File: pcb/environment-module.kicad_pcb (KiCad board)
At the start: 4 copper layers, 50 x 25 mm, 100 parts, among them J1 AVR-UPDI-6, U1 ATtiny1616-MNR, U2 PCA9545APW, U3 AHT20-F, U4 LTR-303ALS-01, U5 SGP40-D-R4

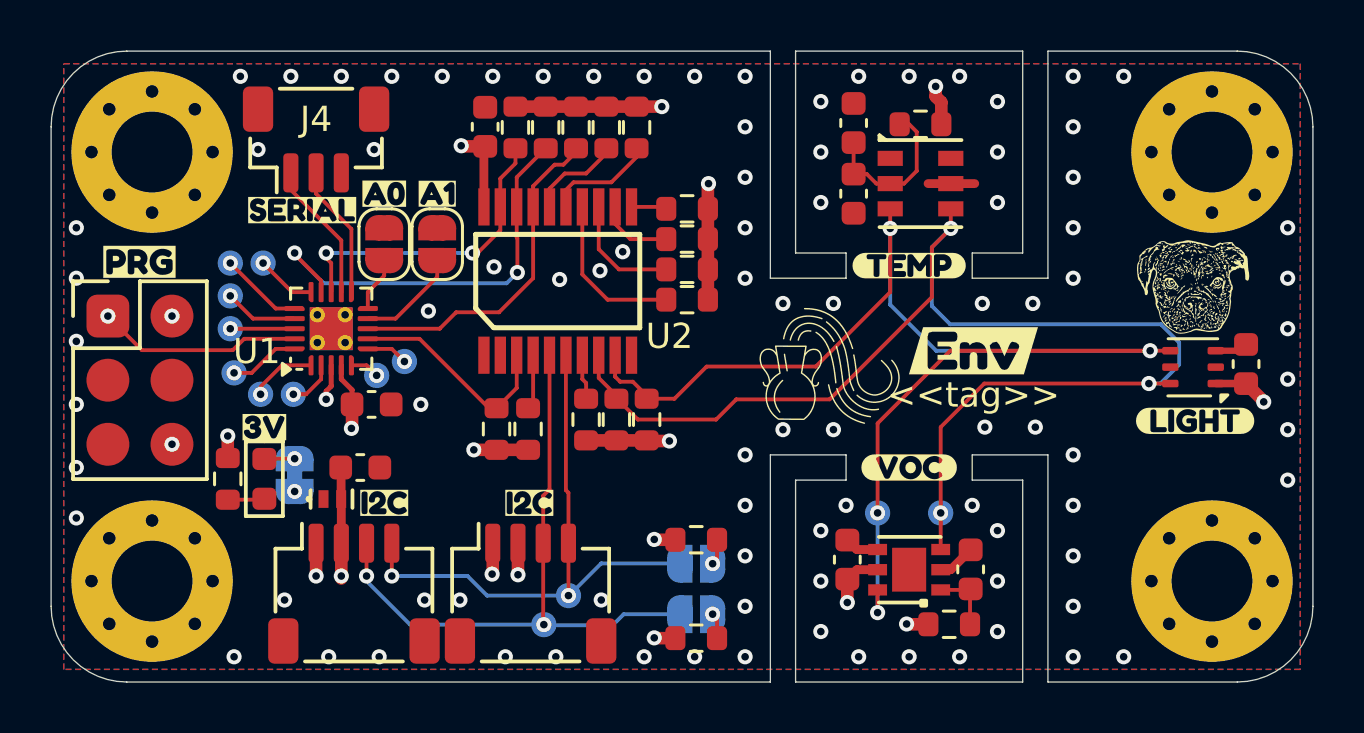
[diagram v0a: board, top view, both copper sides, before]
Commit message: Updated UPDI Connector
Integrated serial and UPDI
Changed to vertical connectors
Updated renders
Rounded cutouts
Adjusted silkscreen
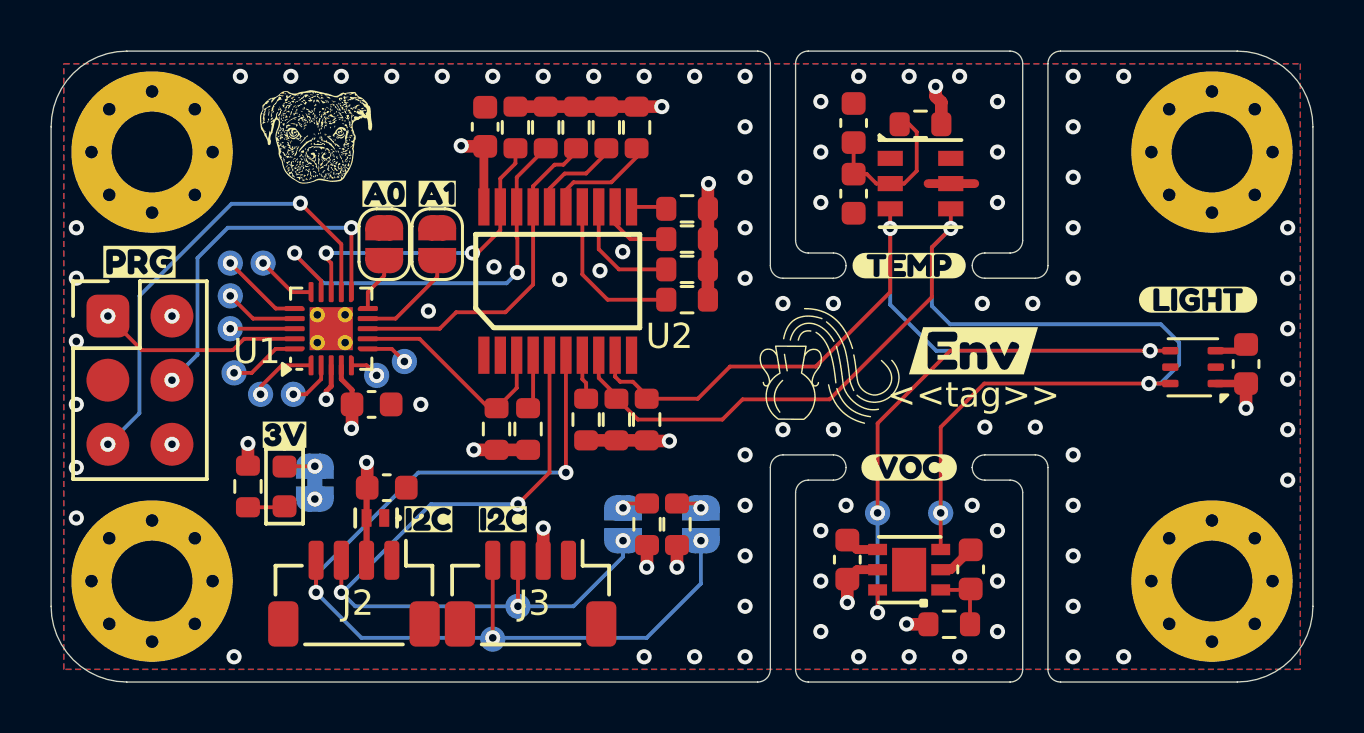
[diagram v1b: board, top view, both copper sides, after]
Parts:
- removed J4: ~, CRGM Connector:JST_SH_BM03B-SRSS-TB_1x03-1MP_P1.00mm_Vertical
- removed kibuzzard-68FC4AED: G***, kibuzzard-68FC4AED
- removed kibuzzard-68FC4C30: G***, kibuzzard-68FC4C30
- removed kibuzzard-690D67C0: G***, kibuzzard-690D67C0
- removed kibuzzard-690D67CF: G***, kibuzzard-690D67CF
- added kibuzzard-69C852D5: G***, kibuzzard-69C852D5, B.Cu at (58.6, 134.8)
- added kibuzzard-69C852DC: G***, kibuzzard-69C852DC, B.Cu at (58.6, 136.0)
- added kibuzzard-69C852F0: G***, kibuzzard-69C852F0, B.Cu at (54.8, 141.8)
- J2, J3: footprint CRGM Connector:JST_SH_SM04B-SRSS-TB_1x04-1MP_P1.00mm_Horizontal -> CRGM Connector:JST_SH_BM04B-SRSS-TB_1x04-1MP_P1.00mm_Vertical
- moved LOGO5 35.3 mm to (60.5, 128.5)
- moved LOGO1 28.8 mm to (90.2, 137.5)
- moved kibuzzard-68F7F6D5 5.59 mm to (72.7, 141.8)
- moved kibuzzard-690D6835 5.38 mm to (65.0, 148.2), turned to 180 degrees
- moved R3 4.92 mm to (73.6, 143.8), turned to -90 degrees
- moved kibuzzard-6952D1FF 4.80 mm to (95.5, 134.8)
- moved JP4 4.59 mm to (72.7, 143.8), turned to 90 degrees
- moved kibuzzard-68F7F6E1 4.15 mm to (75.8, 141.8)
- moved TP13 3.46 mm to (67.5, 148.3)
- moved kibuzzard-691D233B 3.06 mm to (84.5, 137.2)
- moved kibuzzard-6908DD87 2.02 mm to (58.6, 142.1)
- moved kibuzzard-68FAFCDC 1.87 mm to (65.0, 143.6)
- moved D2 1.86 mm to (62.9, 143.5), turned to 180 degrees
- moved JP3 1.57 mm to (75.8, 143.8), turned to 90 degrees
- moved kibuzzard-690D683A 1.50 mm to (65.5, 147.0)
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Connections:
- J1 pad 4: unconnected-(J1-NC-Pad4) -> RXD
- J1 pad 5: unconnected-(J1-NC-Pad5) -> TXD
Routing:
- net EXT_SCL: track 23.7 -> 39.9 mm, vias 2 -> 4
- net TXD: track 4.88 -> 18.5 mm, vias 0 -> 2
- net RXD: track 5.30 -> 14.4 mm, vias 0 -> 2
- net EXT_SDA: track 26.1 -> 30.8 mm, vias 2 -> 4
- net GND: track 9.64 -> 7.10 mm, vias 96 -> 84
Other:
- outline, holes or cut-outs redrawn

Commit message: Closed #3
Added status LEDs -- updated
Updated renders
Updated silkscreen
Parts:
- removed TP1, TP2, TP3: ~, CRGM Mechanical:TestPoint_Pad_D1.0mm
- removed kibuzzard-68FC4C43: G***, kibuzzard-68FC4C43
- removed kibuzzard-690D67F2: G***, kibuzzard-690D67F2
- removed kibuzzard-6951AF60: G***, kibuzzard-6951AF60
- removed kibuzzard-6951AF68: G***, kibuzzard-6951AF68
- removed kibuzzard-69C852D5: G***, kibuzzard-69C852D5
- added D3: Blue, CRGM Passive:LED_0603_1608Metric, F.Cu at (58.5, 128.0)
- added D4: Blue, CRGM Passive:LED_0603_1608Metric, F.Cu at (61.4, 128.0)
- added D9: Blue, CRGM Passive:LED_0603_1608Metric, F.Cu at (64.2, 128.0)
- added R15: 1K, CRGM Passive:R_0603_1608Metric, F.Cu at (59.9, 128.0)
- added R20: 1K, CRGM Passive:R_0603_1608Metric, F.Cu at (65.7, 128.0)
- added R22: 1K, CRGM Passive:R_0603_1608Metric, F.Cu at (62.8, 128.0)
- added kibuzzard-69DC4F14: G***, kibuzzard-69DC4F14, F.Cu at (58.5, 125.8)
- added kibuzzard-69DC4F1F: G***, kibuzzard-69DC4F1F, F.Cu at (61.4, 125.9)
- added kibuzzard-69DC4F46: G***, kibuzzard-69DC4F46, F.Cu at (64.2, 125.8)
- added kibuzzard-69DC5370: G***, kibuzzard-69DC5370, B.Cu at (56.4, 134.0)
- added kibuzzard-69DC53A1: G***, kibuzzard-69DC53A1, B.Cu at (58.8, 139.8)
- moved LOGO5 31.5 mm to (90.6, 137.6)
- moved LOGO2 2.05 mm to (78.5, 137.9), turned to 0 degrees
- moved kibuzzard-69029C60 2.05 mm to (84.5, 136.9)
- moved kibuzzard-690D67E0 1.26 mm to (56.2, 138.8), turned to -135 degrees
- moved kibuzzard-69571EDB 0.86 mm to (57.3, 139.7), turned to -135 degrees
- moved R1 0.40 mm to (71.2, 140.0)
- moved R17 0.40 mm to (72.4, 140.0)
- moved R18 0.40 mm to (73.6, 140.0)
- moved LOGO1 0.23 mm to (90.0, 137.6), turned to 180 degrees
- moved kibuzzard-691D233B 0.23 mm to (84.4, 137.4)
- moved R14 0.06 mm to (68.3, 128.0)
- moved C6 0.06 mm to (67.2, 128.0)
- moved R10 0.06 mm to (73.2, 128.0)
- moved R11 0.06 mm to (72.0, 128.0)
- moved R12 0.06 mm to (70.8, 128.0)
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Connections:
- U1 pad 15: /MCU/PC0 -> LED_VOC
- U1 pad 16: /MCU/PC1 -> LED_LIGHT
- U1 pad 17: /MCU/PC2 -> LED_TEMP
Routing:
- net LED_VOC: track 0.00 -> 11.0 mm
- net LED_LIGHT: track 0.00 -> 8.88 mm
- net LED_TEMP: track 0.00 -> 8.25 mm
- net /MCU/PC1: track 3.30 -> 0.00 mm, vias 1 -> 0
- net /MCU/PC2: track 2.92 -> 0.00 mm, vias 1 -> 0
- net /MCU/PC0: track 2.38 -> 0.00 mm, vias 1 -> 0
- net +3.3V: track 36.5 -> 38.2 mm, vias 16 -> 19
- net RXD: track 14.4 -> 12.8 mm
- net Net-(D9-A): track 0.00 -> 1.41 mm
- net Net-(D4-A): track 0.00 -> 1.41 mm
- net Net-(D3-A): track 0.00 -> 1.41 mm
- net MCU_SCL: track 16.9 -> 15.8 mm
- net TXD: track 18.5 -> 17.6 mm
- net /Peripherals/INT_SDA: track 51.4 -> 52.0 mm
- net EXT_SDA: vias 4 -> 3
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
